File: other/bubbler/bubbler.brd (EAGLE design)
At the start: 95.2 x 63.5 mm, 73 parts, among them SW1 SWITCH-DIP-GDH-02, SW2 ITT-SWITCH-KSS-G, U1 STM32F41X-100P, U2 SPANSION-S25FL256, U3 LM4890, U4 BIPOLAR-PMBT6428, U5 USBLC6-2, U6 TLV1117, U7 MOLEX-1.25-WTB-RA-CONN-2POS, X2 CM415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

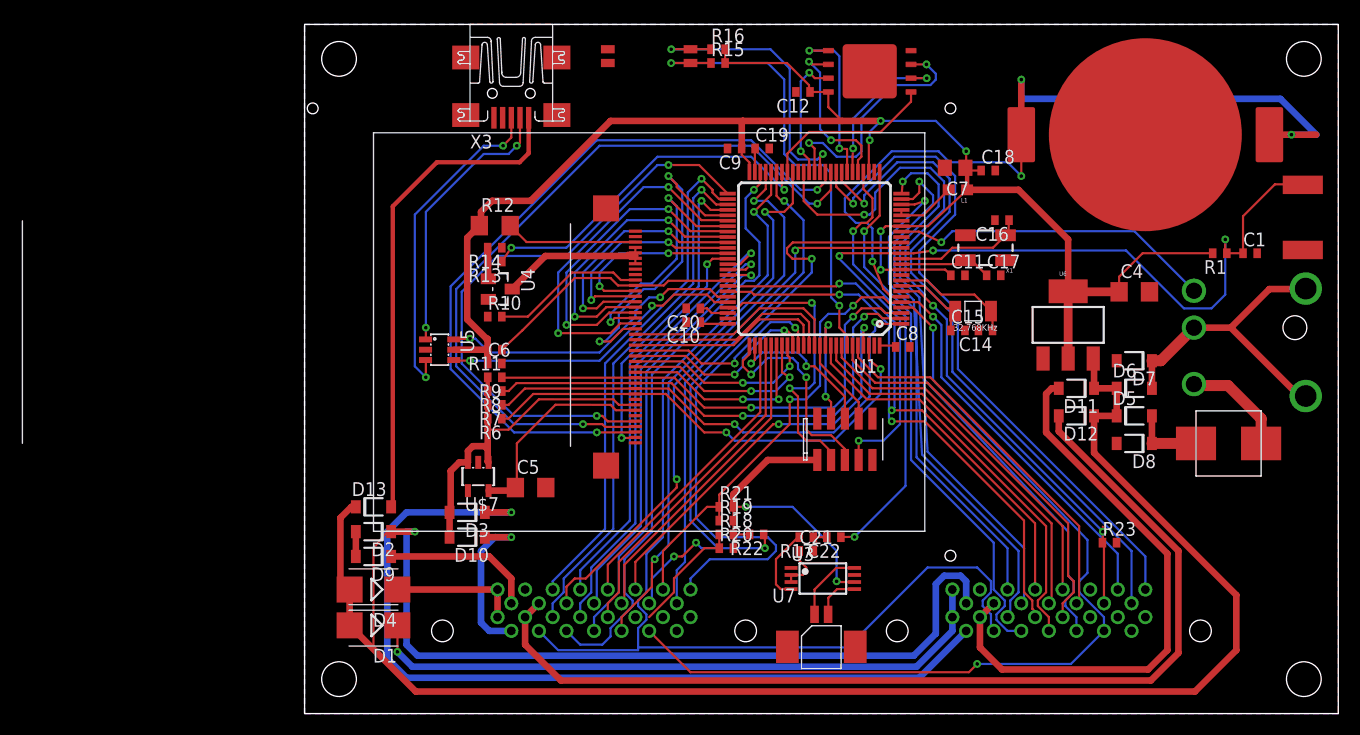
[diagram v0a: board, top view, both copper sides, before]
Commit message: Clean up bubbler board.
Just small routing changes.
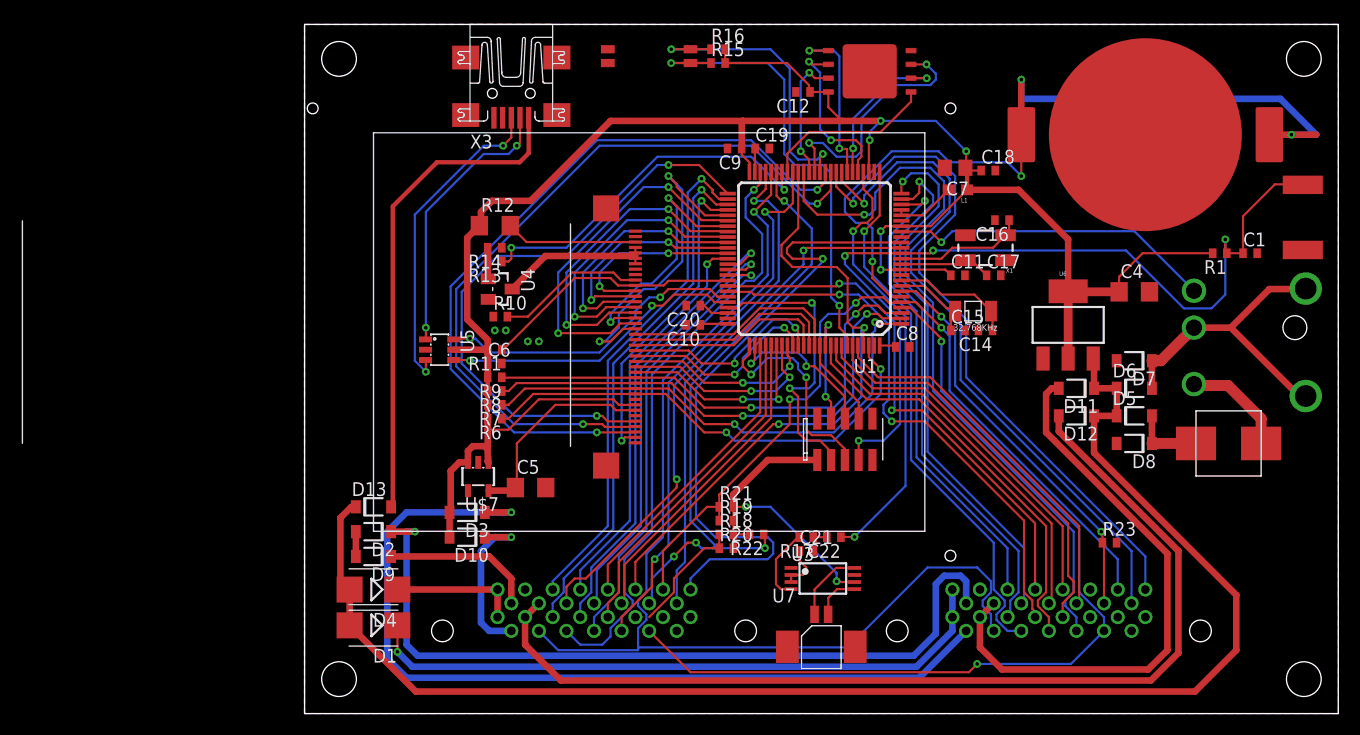
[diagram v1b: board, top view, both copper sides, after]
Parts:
- moved R10 0.51 mm to (18.0, 36.6)
- moved C10 0.25 mm to (35.8, 35.8)
- moved C20 0.25 mm to (35.8, 37.6)
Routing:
- net EXT1_12: track 37.8 -> 58.9 mm
- net N$22: track 87.9 -> 73.3 mm
- net CARD0_INSERT: track 39.3 -> 37.3 mm
- net N$10: track 15.6 -> 14.1 mm
- net CARD1_INSERT: track 56.9 -> 58.2 mm
- net N$13: track 4.13 -> 2.89 mm
- net EXT1_ADC1: track 60.9 -> 62.1 mm
- net 3.3V: track 228.3 -> 227.1 mm
- net N$6: track 30.7 -> 29.6 mm
- net NRST: track 80.8 -> 79.9 mm
- net CARD_SCL: track 94.8 -> 94.2 mm
- net N$4: track 14.3 -> 13.8 mm
